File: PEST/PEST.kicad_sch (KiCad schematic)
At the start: 4 parts, among them J1 Conn_01x01, J2 Conn_01x01, J3 Conn_01x01, J4 Conn_01x01

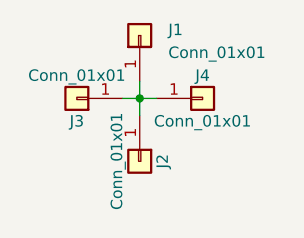
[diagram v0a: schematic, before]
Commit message: Updated PEST for SMD mounting
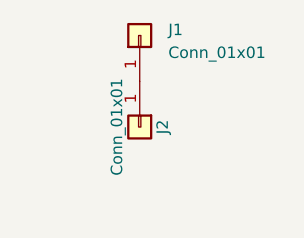
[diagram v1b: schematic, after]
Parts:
- removed J3, J4: Conn_01x01, PEST:Bridge_Pad, symbol Connector_Generic:Conn_01x01
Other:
- moved on the sheet: J2
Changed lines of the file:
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@@
 (kicad_sch (version 20230121) (generator eeschema)
   (paper "A4")
-  (junction (at 26.035 22.86) (diameter 0) (color 0 0 0 0)
-  )
-  (wire (pts (xy 24.13 22.86) (xy 26.035 22.86))
-    (stroke (width 0) (type default))
-  )
-  (wire (pts (xy 26.035 20.955) (xy 26.035 22.86))
-    (stroke (width 0) (type default))
-  )
-  (wire (pts (xy 26.035 22.86) (xy 27.94 22.86))
-    (stroke (width 0) (type default))
-  )
-  (wire (pts (xy 26.035 22.86) (xy 26.035 24.765))
-    (stroke (width 0) (type default))
-  )
   (symbol (lib_id "Connector_Generic:Conn_01x01") (at 26.035 15.875 90) (unit 1)
     (in_bom yes) (on_board yes) (dnp no) (fields_autoplaced)
@@
     )
   )
-  (symbol (lib_id "Connector_Generic:Conn_01x01") (at 26.035 29.845 270) (unit 1)
+  (symbol (lib_id "Connector_Generic:Conn_01x01") (at 26.035 26.035 270) (unit 1)
     (in_bom yes) (on_board yes) (dnp no)
-    (property "Reference" "J2" (at 28.575 29.845 0)
+    (property "Reference" "J2" (at 28.575 26.035 0)
       (effects (font (size 1.27 1.27)))
     )
-    (property "Value" "Conn_01x01" (at 23.495 29.845 0)
+    (property "Value" "Conn_01x01" (at 23.495 26.035 0)
       (effects (font (size 1.27 1.27)))
     )
-    (property "Footprint" "PEST:Bridge_Pad" (at 26.035 29.845 0)
+    (property "Footprint" "PEST:Bridge_Pad" (at 26.035 26.035 0)
       (effects (font (size 1.27 1.27)) hide)
     )
-    (property "Datasheet" "~" (at 26.035 29.845 0)
+    (property "Datasheet" "~" (at 26.035 26.035 0)
       (effects (font (size 1.27 1.27)) hide)
     )
@@
         )
       )
-    )
-  )
-  (symbol (lib_id "Connector_Generic:Conn_01x01") (at 33.02 22.86 0) (unit 1)
-    (in_bom yes) (on_board yes) (dnp no)
-    (property "Reference" "J4" (at 33.02 20.32 0)
-      (effects (font (size 1.27 1.27)))
-    )
-    (property "Value" "Conn_01x01" (at 33.02 25.4 0)
-      (effects (font (size 1.27 1.27)))
-    )
-    (property "Footprint" "PEST:Bridge_Pad" (at 33.02 22.86 0)
-      (effects (font (size 1.27 1.27)) hide)
-    )
-    (property "Datasheet" "~" (at 33.02 22.86 0)
-      (effects (font (size 1.27 1.27)) hide)
-    )
-    (pin "1")
-    (instances
-      (project "PEST"
-        (path "/c600406e-1969-4a0f-bdff-48903ca0b9f9"
-          (reference "J4") (unit 1)
-        )
-      )
-    )
-  )
-  (symbol (lib_id "Connector_Generic:Conn_01x01") (at 19.05 22.86 180) (unit 1)
-    (in_bom yes) (on_board yes) (dnp no)
-    (property "Reference" "J3" (at 19.05 25.4 0)
-      (effects (font (size 1.27 1.27)))
-    )
-    (property "Value" "Conn_01x01" (at 19.05 20.32 0)
-      (effects (font (size 1.27 1.27)))
-    )
-    (property "Footprint" "PEST:Bridge_Pad" (at 19.05 22.86 0)
-      (effects (font (size 1.27 1.27)) hide)
-    )
-    (property "Datasheet" "~" (at 19.05 22.86 0)
-      (effects (font (size 1.27 1.27)) hide)
-    )
-    (pin "1")
-    (instances
-      (project "PEST"
-        (path "/c600406e-1969-4a0f-bdff-48903ca0b9f9"
-          (reference "J3") (unit 1)
-        )
-      )

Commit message: Fixed some PEST tile glitches
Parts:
- J1, J2: footprint PEST:Bridge_Pad -> Touchstone:Bridge_Pad
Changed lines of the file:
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@@
       (effects (font (size 1.27 1.27)) (justify right))
     )
-    (property "Footprint" "PEST:Bridge_Pad" (at 26.035 15.875 0)
+    (property "Footprint" "Touchstone:Bridge_Pad" (at 26.035 15.875 0)
       (effects (font (size 1.27 1.27)) hide)
     )
@@
       (effects (font (size 1.27 1.27)))
     )
-    (property "Footprint" "PEST:Bridge_Pad" (at 26.035 26.035 0)
+    (property "Footprint" "Touchstone:Bridge_Pad" (at 26.035 26.035 0)
       (effects (font (size 1.27 1.27)) hide)
     )
